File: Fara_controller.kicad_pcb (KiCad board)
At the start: 2 copper layers, 69.3 x 84 mm, 54 parts, among them U1 XL1509-12, U2 XL1509-05, U3 LDD-700L, U4 LDD-700L, U6 LDD-700L, U7 LDD-700L, U8 LDD-700L, U9 LDD-700L, X1 Conn_01x02, X10 Conn_01x02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

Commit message: v0.2 draft decomposition was made
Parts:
- removed U7, U8, U9: LDD-700L, my8lib:LDD-700L
- removed X15, X16, X17: Conn_01x02, Connector_JST:JST_XH_B2B-XH-A_1x02_P2.50mm_Vertical
- added C10: 0.22 uF, Capacitor_SMD:C_0603_1608Metric_Pad1.08x0.95mm_HandSolder, F.Cu at (86.3, 34.7)
- added C11: 0.22 uF, Capacitor_SMD:C_0603_1608Metric_Pad1.08x0.95mm_HandSolder, F.Cu at (85.0, 46.0)
- added C12: 0.22 uF, Capacitor_SMD:C_0603_1608Metric_Pad1.08x0.95mm_HandSolder, F.Cu at (85.5, 58.4)
- added C13: 4u7, Capacitor_SMD:C_0805_2012Metric_Pad1.18x1.45mm_HandSolder, F.Cu at (82.5, 32.0)
- added C14: 4u7, Capacitor_SMD:C_0805_2012Metric_Pad1.18x1.45mm_HandSolder, F.Cu at (81.1, 43.0)
- added C15: 4u7, Capacitor_SMD:C_0805_2012Metric_Pad1.18x1.45mm_HandSolder, F.Cu at (81.6, 55.6)
- added C7: 1u, Capacitor_SMD:C_0603_1608Metric_Pad1.08x0.95mm_HandSolder, F.Cu at (86.2, 37.3)
- added C8: 1u, Capacitor_SMD:C_0603_1608Metric_Pad1.08x0.95mm_HandSolder, F.Cu at (84.8, 48.4)
- added C9: 1u, Capacitor_SMD:C_0603_1608Metric_Pad1.08x0.95mm_HandSolder, F.Cu at (85.3, 60.9)
- added L3: 22uH, Inductor_SMD:L_7.3x7.3_H4.5, F.Cu at (76.4, 34.9)
- added L4: 22uH, Inductor_SMD:L_7.3x7.3_H4.5, F.Cu at (75.0, 45.9)
- added L5: 22uH, Inductor_SMD:L_7.3x7.3_H4.5, F.Cu at (75.5, 58.4)
- added R10: 1 Ohm, Resistor_SMD:R_0603_1608Metric_Pad0.98x0.95mm_HandSolder, F.Cu at (87.3, 31.1)
- added R11: 1 Ohm, Resistor_SMD:R_0603_1608Metric_Pad0.98x0.95mm_HandSolder, F.Cu at (85.7, 31.1)
- added R12: 1 Ohm, Resistor_SMD:R_0603_1608Metric_Pad0.98x0.95mm_HandSolder, F.Cu at (92.0, 43.3)
- added R13: 1 Ohm, Resistor_SMD:R_0603_1608Metric_Pad0.98x0.95mm_HandSolder, F.Cu at (90.4, 43.4)
- added R14: 1 Ohm, Resistor_SMD:R_0603_1608Metric_Pad0.98x0.95mm_HandSolder, F.Cu at (88.8, 43.4)
- added R15: 1 Ohm, Resistor_SMD:R_0603_1608Metric_Pad0.98x0.95mm_HandSolder, F.Cu at (84.2, 43.4)
- added R16: 1 Ohm, Resistor_SMD:R_0603_1608Metric_Pad0.98x0.95mm_HandSolder, F.Cu at (85.7, 43.4)
- added R17: 1 Ohm, Resistor_SMD:R_0603_1608Metric_Pad0.98x0.95mm_HandSolder, F.Cu at (87.3, 43.3)
- added R18: 1 Ohm, Resistor_SMD:R_0603_1608Metric_Pad0.98x0.95mm_HandSolder, F.Cu at (92.2, 54.7)
- added R19: 1 Ohm, Resistor_SMD:R_0603_1608Metric_Pad0.98x0.95mm_HandSolder, F.Cu at (90.6, 54.7)
- added R20: 1 Ohm, Resistor_SMD:R_0603_1608Metric_Pad0.98x0.95mm_HandSolder, F.Cu at (89.0, 54.7)
- added R21: 1 Ohm, Resistor_SMD:R_0603_1608Metric_Pad0.98x0.95mm_HandSolder, F.Cu at (87.5, 54.8)
- added R22: 1 Ohm, Resistor_SMD:R_0603_1608Metric_Pad0.98x0.95mm_HandSolder, F.Cu at (85.9, 54.8)
- added R23: 1 Ohm, Resistor_SMD:R_0603_1608Metric_Pad0.98x0.95mm_HandSolder, F.Cu at (84.3, 54.8)
- added R9: 1 Ohm, Resistor_SMD:R_0603_1608Metric_Pad0.98x0.95mm_HandSolder, F.Cu at (88.9, 31.2)
- added VD4: CDBA3100-HF, Diode_SMD:D_SOD-123, F.Cu at (82.9, 38.0)
- added VD5: CDBA3100-HF, Diode_SMD:D_SOD-123, F.Cu at (81.6, 48.9)
- added VD6: CDBA3100-HF, Diode_SMD:D_SOD-123, F.Cu at (82.1, 61.5)
- R4, R5, R6: value 10k -> 1 Ohm
- U3, U4, U6: value LDD-700L -> TPS61165DBV; footprint my8lib:LDD-700L -> Package_TO_SOT_SMD:SOT-23-6
- VD1, VD3: footprint Diode_SMD:D_SMA -> Diode_SMD:D_SOD-123
- moved R6 56.7 mm to (90.5, 31.1), turned to -90 degrees
- moved R5 48.8 mm to (92.2, 31.1), turned to -90 degrees
- moved R4 41.4 mm to (93.8, 31.1), turned to -90 degrees
- moved R1 20.7 mm to (82.2, 30.1), turned to 0 degrees
- moved R2 17.4 mm to (81.1, 41.2), turned to 0 degrees
- moved R3 17.1 mm to (81.5, 53.8), turned to 0 degrees
- moved U6 10.7 mm to (81.7, 58.4)
- moved U3 9.41 mm to (82.5, 34.8)
- moved U4 8.79 mm to (81.3, 45.8)
- moved X13 6.63 mm to (89.9, 48.2), turned to 0 degrees
- moved X14 6.04 mm to (90.2, 59.4), turned to 0 degrees
- moved X12 4.54 mm to (91.0, 36.0), turned to 0 degrees
- moved VD3 0.74 mm to (49.9, 37.8)
- moved VD1 0.71 mm to (32.9, 31.5)
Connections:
- R4 pad 1: LEDS4 -> GND
- R4 pad 2: GND -> Net-(U3-FB)
- R5 pad 1: LEDS5 -> GND
- R5 pad 2: GND -> Net-(U3-FB)
- R6 pad 1: LEDS6 -> GND
- R6 pad 2: GND -> Net-(U3-FB)
- U3 pad 3: GND -> Net-(U3-SW)
- U3 pad 4: Net-(U3-Vout-) -> GND
- U3 pad 5: Net-(U3-Vout+) -> Net-(U3-COMP)
- U4 pad 3: GND -> Net-(U4-SW)
- U4 pad 4: Net-(U4-Vout-) -> GND
- U4 pad 5: Net-(U4-Vout+) -> Net-(U4-COMP)
- U6 pad 3: GND -> Net-(U6-SW)
- U6 pad 4: Net-(U6-Vout-) -> GND
- U6 pad 5: Net-(U6-Vout+) -> Net-(U6-COMP)
- X12 pad 1: Net-(U3-Vout+) -> Net-(VD4-K)
- X12 pad 2: Net-(U3-Vout-) -> Net-(U3-FB)
- X13 pad 1: Net-(U4-Vout+) -> Net-(VD5-K)
- X13 pad 2: Net-(U4-Vout-) -> Net-(U4-FB)
- X14 pad 1: Net-(U6-Vout+) -> Net-(VD6-K)
- X14 pad 2: Net-(U6-Vout-) -> Net-(U6-FB)
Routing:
- net VPP: track 148.5 -> 74.8 mm
- net Net-(U9-Vout+): track 14.7 -> 0.00 mm
- net Net-(U8-Vout+): track 14.7 -> 0.00 mm
- net Net-(U6-Vout+): track 14.2 -> 0.00 mm
- net Net-(U7-Vout+): track 13.5 -> 0.00 mm
- net Net-(U3-Vout+): track 12.6 -> 0.00 mm
- net Net-(U4-Vout+): track 12.4 -> 0.00 mm
- net Net-(U8-Vout-): track 11.1 -> 0.00 mm
- net Net-(U9-Vout-): track 10.5 -> 0.00 mm
- net Net-(U7-Vout-): track 10.4 -> 0.00 mm
- net Net-(U6-Vout-): track 10.3 -> 0.00 mm
- net Net-(U4-Vout-): track 9.80 -> 0.00 mm
- net Net-(U3-Vout-): track 9.57 -> 0.00 mm
- net Net-(U1-OUT): track 9.37 -> 8.51 mm
- net Net-(U2-OUT): track 12.6 -> 12.0 mm

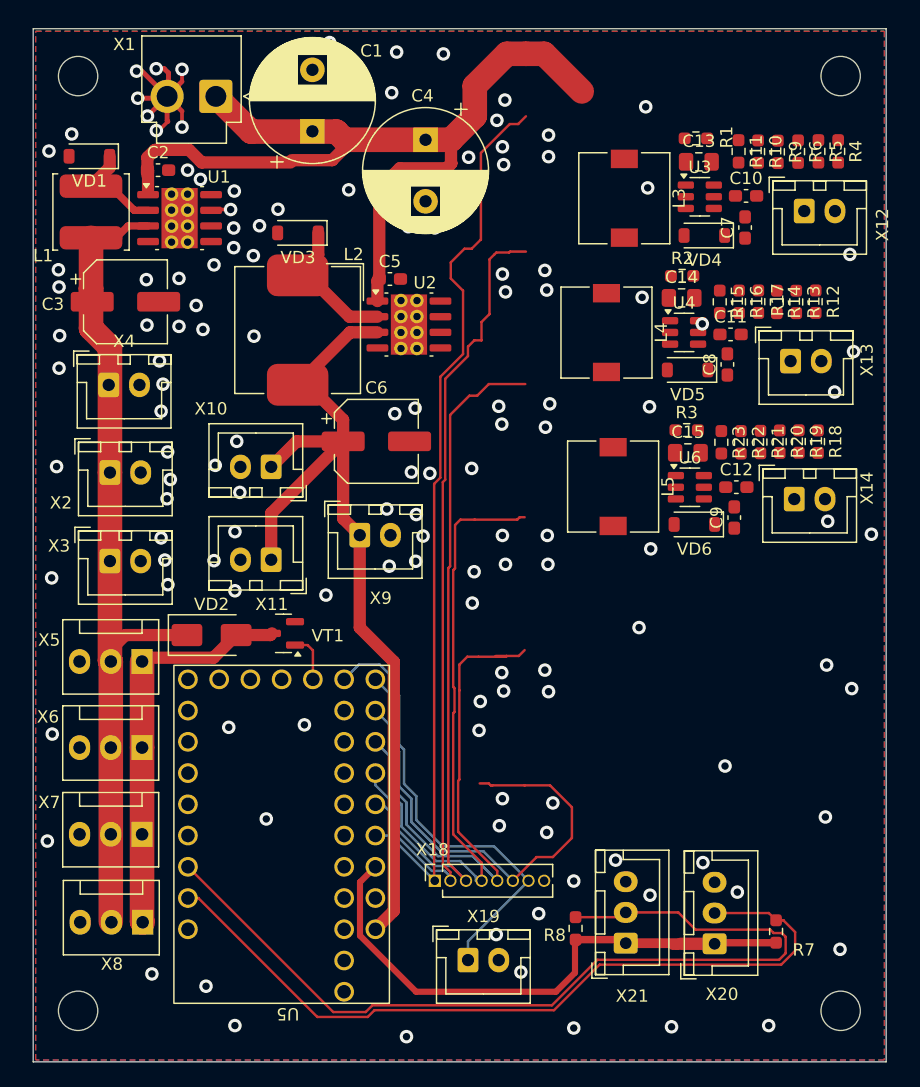
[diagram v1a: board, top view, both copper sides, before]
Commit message: v0.3 4th driver was decomposed
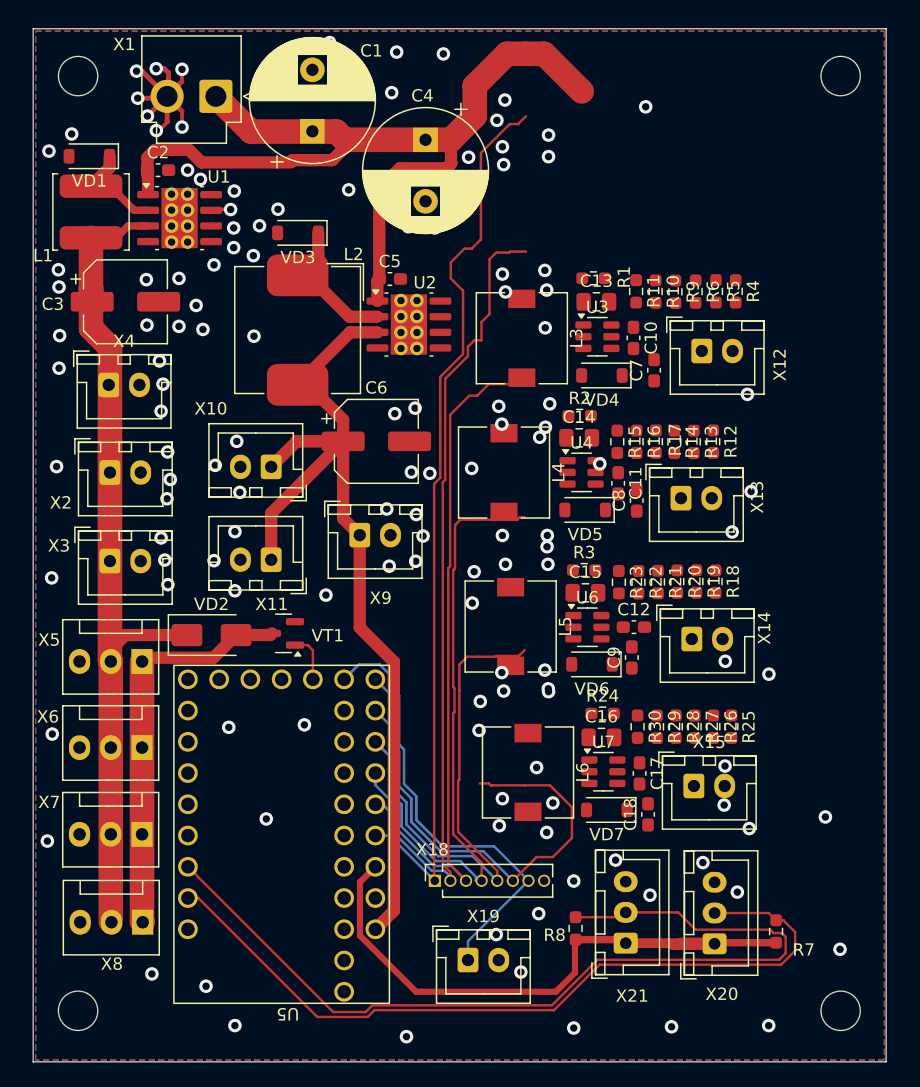
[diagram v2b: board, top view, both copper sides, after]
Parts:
- added C16: 4u7, Capacitor_SMD:C_0805_2012Metric_Pad1.18x1.45mm_HandSolder, F.Cu at (74.5, 78.8)
- added C17: 0.22 uF, Capacitor_SMD:C_0603_1608Metric_Pad1.08x0.95mm_HandSolder, F.Cu at (77.7, 81.7)
- added C18: 1u, Capacitor_SMD:C_0603_1608Metric_Pad1.08x0.95mm_HandSolder, F.Cu at (78.3, 85.0)
- added L6: 22uH, Inductor_SMD:L_7.3x7.3_H4.5, F.Cu at (68.6, 81.6)
- added R24: 10k, Resistor_SMD:R_0603_1608Metric_Pad0.98x0.95mm_HandSolder, F.Cu at (74.7, 76.8)
- added R25: 1 Ohm, Resistor_SMD:R_0603_1608Metric_Pad0.98x0.95mm_HandSolder, F.Cu at (85.1, 77.9)
- added R26: 1 Ohm, Resistor_SMD:R_0603_1608Metric_Pad0.98x0.95mm_HandSolder, F.Cu at (83.7, 77.9)
- added R27: 1 Ohm, Resistor_SMD:R_0603_1608Metric_Pad0.98x0.95mm_HandSolder, F.Cu at (82.1, 77.9)
- added R28: 1 Ohm, Resistor_SMD:R_0603_1608Metric_Pad0.98x0.95mm_HandSolder, F.Cu at (80.6, 77.9)
- added R29: 1 Ohm, Resistor_SMD:R_0603_1608Metric_Pad0.98x0.95mm_HandSolder, F.Cu at (79.1, 77.9)
- added R30: 1 Ohm, Resistor_SMD:R_0603_1608Metric_Pad0.98x0.95mm_HandSolder, F.Cu at (77.5, 77.9)
- added U7: TPS61165DBV, Package_TO_SOT_SMD:SOT-23-6, F.Cu at (74.7, 81.6)
- added VD7: CDBA3100-HF, Diode_SMD:D_SOD-123, F.Cu at (75.0, 84.7)
- added X15: Conn_01x02, Connector_JST:JST_XH_B2B-XH-A_1x02_P2.50mm_Vertical, F.Cu at (82.1, 82.7)
- moved C11 15.2 mm to (75.9, 58.1), turned to -90 degrees
- moved C10 14.7 mm to (77.2, 46.3), turned to -90 degrees
- moved X13 14.3 mm to (81.0, 59.3)
- moved R10 14.1 mm to (79.0, 42.5)
- moved R6 14.1 mm to (82.2, 42.5)
- moved X12 14.1 mm to (82.7, 47.4)
- moved R9 14.1 mm to (80.6, 42.5)
- moved C12 14.1 mm to (77.2, 69.8)
- moved C13 14.1 mm to (74.1, 43.4)
- moved C9 14.1 mm to (77.0, 72.3)
- moved L3 14.1 mm to (68.1, 46.3)
- moved R13 14.1 mm to (82.1, 54.7)
- moved R14 14.1 mm to (80.5, 54.7)
- moved R18 14.1 mm to (83.8, 66.1)
- moved R21 14.1 mm to (79.2, 66.1)
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
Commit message: v0.4 draft routing was completed
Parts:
- moved C1 14.0 mm to (62.2, 38.0)
- moved C4 13.5 mm to (71.3, 37.9), turned to 45 degrees
- moved X1 9.34 mm to (50.6, 32.3), turned to 90 degrees
- moved C9 5.48 mm to (82.5, 72.1)
- moved X13 5.01 mm to (86.0, 58.5)
- moved REF** 5.00 mm to (89.0, 101.0)
- moved REF** 5.00 mm to (89.0, 25.0)
- moved R12 4.78 mm to (88.3, 53.7)
- moved R13 4.78 mm to (86.7, 53.8)
- moved R14 4.78 mm to (85.2, 53.8)
- moved R17 4.78 mm to (83.7, 53.7)
- moved R15 4.78 mm to (80.5, 53.7)
- moved R16 4.78 mm to (82.1, 53.7)
- moved C11 4.66 mm to (80.5, 57.1)
- moved C17 4.56 mm to (82.2, 81.1)
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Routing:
- net VPP: track 74.8 -> 191.9 mm
- net LEDS5: track 45.2 -> 19.6 mm
- net LEDS6: track 40.1 -> 23.0 mm
- net Net-(U3-FB): track 0.00 -> 14.9 mm
- net Net-(U6-FB): track 0.00 -> 14.3 mm
- net Net-(U7-FB): track 0.00 -> 14.2 mm
- net Net-(U4-FB): track 0.00 -> 14.1 mm
- net LEDS4: track 52.3 -> 42.8 mm
- net Net-(U4-SW): track 0.00 -> 8.27 mm
- net Net-(U3-SW): track 0.00 -> 8.25 mm
- net Net-(U7-SW): track 0.00 -> 8.21 mm
- net Net-(U6-SW): track 0.00 -> 8.14 mm
- net Net-(VD4-K): track 0.00 -> 7.66 mm
- net Net-(VD6-K): track 0.00 -> 7.64 mm
- net Net-(VD5-K): track 0.00 -> 7.27 mm
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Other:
- board size 69.3 x 84 mm -> 64.5 x 84 mm

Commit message: v0.5 actual state
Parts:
- added X16: Conn_01x02, Connector_JST:JST_XH_B2B-XH-A_1x02_P2.50mm_Vertical, F.Cu at (44.0, 42.5)
- moved C1 7.10 mm to (64.6, 31.3), turned to -135 degrees
- moved X1 3.81 mm to (54.4, 32.0), turned to 180 degrees
- moved VD3 2.33 mm to (52.2, 37.8)
- moved C5 2.33 mm to (59.7, 41.5)
- moved L2 2.33 mm to (52.2, 45.7)
- moved U2 2.33 mm to (61.2, 45.2)
- moved C3 1.06 mm to (34.8, 43.2)
- moved REF** 1.00 mm to (89.0, 26.0)
- moved REF** 1.00 mm to (32.0, 26.0)
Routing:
- net GND: track 21.1 -> 1.86 mm, vias 166 -> 169
- net +12V: track 70.2 -> 81.1 mm
- net VPP: track 191.9 -> 194.3 mm
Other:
- board size 64.5 x 84 mm -> 64.5 x 82.7 mm

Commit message: v0.6 actual state
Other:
- board text added: "6x1 Ohm"
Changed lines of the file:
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@@
 		(tags "connector JST XH vertical")
 		(property "Reference" "X15"
-			(at 1.25 -3.55 0)
+			(at 3.175 4.8825 0)
 			(layer "F.SilkS")
 			(effects
@@
 			(at 0 -1.43 90)
 			(layer "F.SilkS")
+			(hide yes)
 			(effects
 				(font
@@
 			(at -0.16 -1.57 90)
 			(layer "F.SilkS")
+			(hide yes)
 			(effects
 				(font
@@
 			(at 0 -1.43 90)
 			(layer "F.SilkS")
+			(hide yes)
 			(effects
 				(font
@@
 			(at 0 -1.43 90)
 			(layer "F.SilkS")
+			(hide yes)
 			(effects
 				(font
@@
 			(at 0 -1.43 90)
 			(layer "F.SilkS")
+			(hide yes)
 			(effects
 				(font
@@
 		(tags "capacitor handsolder")
 		(property "Reference" "C12"
-			(at 0 -1.43 90)
+			(at -0.4175 -1.735 90)
 			(layer "F.SilkS")
 			(effects
@@
 		(tags "capacitor handsolder")
 		(property "Reference" "C15"
-			(at 0 -1.68 0)
+			(at -4.145 -1.742501 0)
 			(layer "F.SilkS")
 			(effects
@@
 			(at 0 -1.43 90)
 			(layer "F.SilkS")
+			(hide yes)
 			(effects
 				(font
@@
 		(tags "capacitor handsolder")
 		(property "Reference" "C16"
-			(at 0 -1.68 0)
+			(at -3.175 -1.8675 0)
 			(layer "F.SilkS")
 			(effects
@@
 		(tags "connector JST XH vertical")
 		(property "Reference" "X14"
-			(at 5.91 -0.89 90)
+			(at 4.865 4.277499 180)
 			(layer "F.SilkS")
 			(effects
@@
 			(at 0 -1.43 90)
 			(layer "F.SilkS")
+			(hide yes)
 			(effects
 				(font
@@
 			(at 0 -1.43 90)
 			(layer "F.SilkS")
+			(hide yes)
 			(effects
 				(font
@@
 			(at 0 -1.43 90)
 			(layer "F.SilkS")
+			(hide yes)
 			(effects
 				(font
@@
 			(at 0.02 -1.42 90)
 			(layer "F.SilkS")
+			(hide yes)
 			(effects
 				(font
@@
 		(tags "SOT TO_SOT_SMD")
 		(property "Reference" "U7"
-			(at 0 -2.4 0)
+			(at -3.145 5.2025 0)
 			(layer "F.SilkS")
 			(effects
@@
 			(at 0 -1.43 90)
 			(layer "F.SilkS")
+			(hide yes)
 			(effects
 				(font
@@
 		(tags "connector JST VH vertical")
 		(property "Reference" "X1"
-			(at 7.45 4.225 360)
+			(at 7.45 4.225 0)
 			(layer "F.SilkS")
 			(effects
@@
 		)
 		(property "Value" "Conn_01x02"
-			(at 1.98 6 360)
+			(at 1.98 6 0)
 			(layer "F.Fab")
 			(hide yes)
@@
 		)
 		(fp_text user "${REFERENCE}"
-			(at 1.98 4.1 360)
+			(at 1.98 4.1 0)
 			(layer "F.Fab")
 			(effects
@@
 		(tags "SOT TO_SOT_SMD")
 		(property "Reference" "U6"
-			(at 0 -2.4 0)
+			(at -4.365 4.909999 0)
 			(layer "F.SilkS")
 			(effects
@@
 			(at 0 -1.43 90)
 			(layer "F.SilkS")
+			(hide yes)
 			(effects
 				(font
@@
 			(at 0 -1.43 90)
 			(layer "F.SilkS")
+			(hide yes)
 			(effects
 				(font
@@
 			(at 0 -1.43 90)
 			(layer "F.SilkS")
+			(hide yes)
 			(effects
 				(font
@@
 			(at 0 -1.43 90)
 			(layer "F.SilkS")
+			(hide yes)
 			(effects
 				(font
@@
 			(at 0 -1.43 90)
 			(layer "F.SilkS")
+			(hide yes)
 			(effects
 				(font
@@
 		(tags "SOD-123")
 		(property "Reference" "VD6"
-			(at 0 -2.000001 0)
+			(at 2.025 -2.027499 0)
 			(layer "F.SilkS")
 			(effects
@@
 		(tags "capacitor handsolder")
 		(property "Reference" "C9"
-			(at 0 -1.43 90)
+			(at -2.1325 -1.045 180)
 			(layer "F.SilkS")
 			(effects
@@
 		(tags "resistor handsolder")
 		(property "Reference" "R3"
-			(at 0 -1.43 0)
+			(at -0.725 -1.312501 0)
 			(layer "F.SilkS")
 			(effects
@@
 			(at 0 -1.43 90)
 			(layer "F.SilkS")
+			(hide yes)
 			(effects
 				(font
@@
 			(at 0 -1.43 90)
 			(layer "F.SilkS")
+			(hide yes)
 			(effects
 				(font
@@
 		(layer "Edge.Cuts")
 	)
+	(gr_text "6x1\nOhm"
+		(at 89.705 68.1225 0)
+		(layer "F.SilkS")
+		(effects
+			(font
+				(size 1 1)
+				(thickness 0.1)
+			)
+			(justify left bottom)
+		)
+	)
+	(gr_text "6x1\nOhm"
+		(at 88.89 55.73 0)
+		(layer "F.SilkS")
+		(effects
+			(font
+				(size 1 1)
+				(thickness 0.1)
+			)
+			(justify left bottom)
+		)
+	)
+	(gr_text "6x1\nOhm"
+		(at 90.03 80.12 0)
+		(layer "F.SilkS")
+		(effects
+			(font
+				(size 1 1)
+				(thickness 0.1)
+			)
+			(justify left bottom)
+		)
+	)
 	(gr_text "Платка Рахилы 70 х 110 мм"
 		(at 29.95 -6.45 0)
@@
 	)
 	(via
-		(at 77.435 63.5975)
+		(at 78.5 63.51)
 		(size 1.1)
 		(drill 0.6)

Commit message: v0.7 small changes
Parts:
- moved X21 1.21 mm to (75.3, 95.5)
- moved R7 1.21 mm to (87.5, 94.6)
- moved X20 1.21 mm to (82.5, 95.6)
- moved C6 0.99 mm to (56.3, 55.7)
- moved R8 0.84 mm to (71.6, 94.2)
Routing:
- net LEDS3: track 52.2 -> 54.4 mm
- net LEDS1: track 72.3 -> 73.3 mm
- net therm1: track 64.3 -> 63.6 mm
- net LEDS2: track 64.6 -> 64.0 mm
- net GND: vias 169 -> 177
